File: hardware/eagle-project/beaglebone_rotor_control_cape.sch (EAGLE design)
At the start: 52 parts, among them IC1 TLC2264CDU, IC2 MCP4901, IC6 TLC2264CDU, Q1 SQ2348ES-T1-GE3, Q2 SQ2348ES-T1-GE3, Q3 SQ2348ES-T1-GE3, Q4 SQ2348ES-T1-GE3, Q5 SQ2348ES-T1-GE3, Q6 SQ2348ES-T1-GE3, U1 TMH0512S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

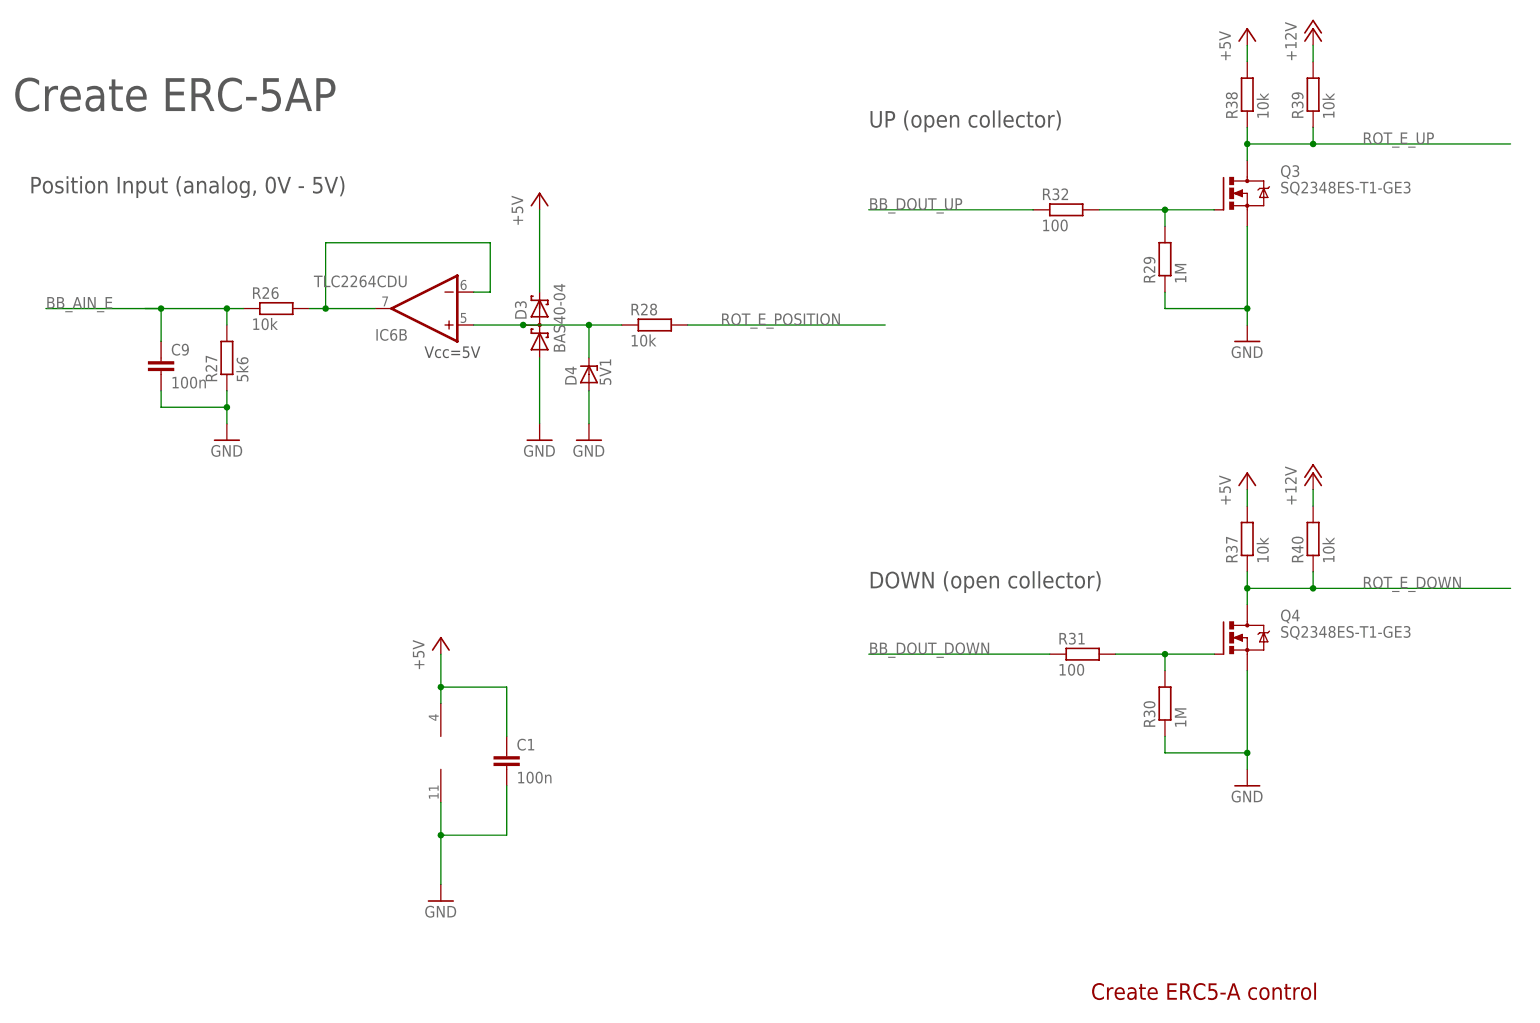
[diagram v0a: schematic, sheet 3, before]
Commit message: Optical tweaks for eagle schematic
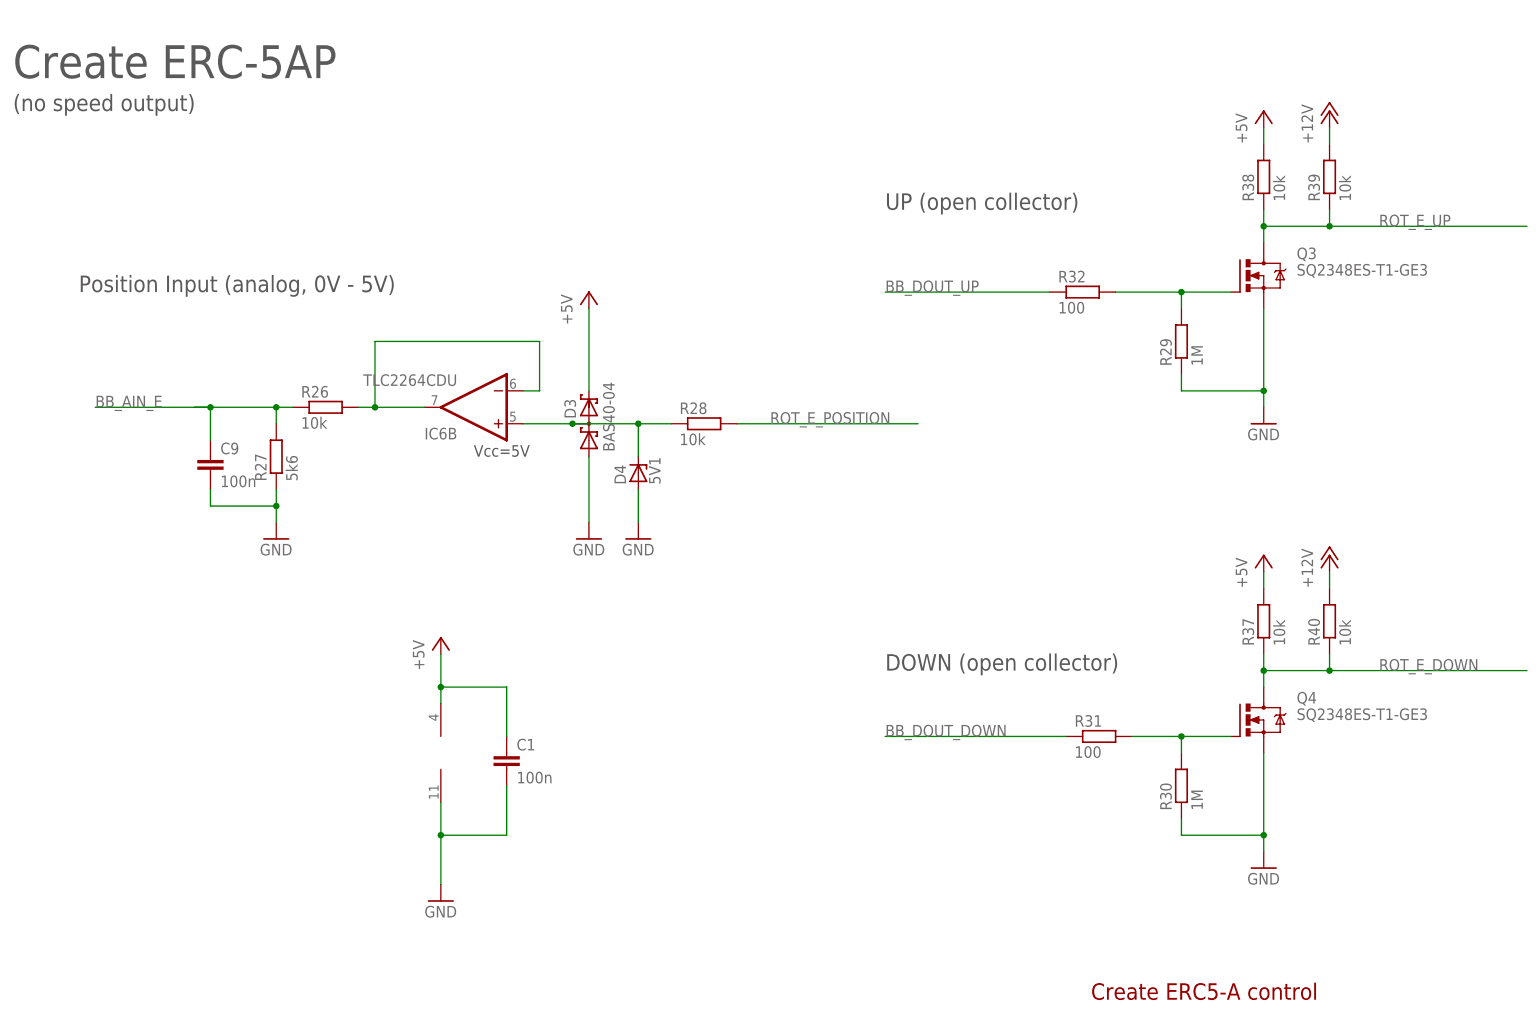
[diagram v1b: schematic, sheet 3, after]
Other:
- note added: "(no speed output)"
- moved on the sheet: C9, D3, D4, IC6B, Q3, Q4, R26, R27, R28, R29, R30, R31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

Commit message: Added serial interface chip to layout
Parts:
- removed R21: 100, rcl:R-EU_R0805
- added C10, C4, C5, C6, C8: 100n, rcl:C-EUC0603
- added IC3: MAX3232ESE, maxim:MAX3232ESE
- added R1, R8: 100, rcl:R-EU_R0805
- added X2: (no value), con-subd:F09VP
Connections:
- removed net BB_SPI0_D1: X1.I2C1_SDA
- removed net BB_SPI1_CS0: X1.SPI1_CS0
- removed net BB_SPI1_D0: X1.SPI1_DO
- removed net BB_SPI1_D1: X1.SPI1_DI
- removed net BB_SPI1_SCLK: X1.SPI1_SCLK
- removed net N$41: X1.EHRPWM2A
- removed net N$42: X1.GPIO1_14
- removed net N$4243: X1.GPIO2_1
- removed net N$43: X1.GPIO0_26
- removed net N$44: X1.GPIO1_12
- removed net N$8: R21.1
- new net BB_UART4_RX: R1.1, X1.UART4_RXD
- new net BB_UART4_TX: R8.1, X1.UART4_TXD
- new net N$16: C4.1, IC3G$1.C2+
- new net N$17: C4.2, IC3G$1.C2-
- new net N$18: C5.2, IC3G$1.C1-
- new net N$19: C5.1, IC3G$1.C1+
- new net N$20: C6.1, IC3G$1.V-
- new net N$21: C8.1, IC3G$1.V+
- new net N$22: IC3G$1.T1IN, R8.2
- new net N$25: IC3G$1.R1OUT, R1.2
- new net RS232_RX: IC3G$1.R1IN, X2.3
- new net RS232_TX: IC3G$1.T1OUT, X2.2
- net +3V3: now also C10.1, IC3P.VCC
- net GND: now also C10.2, C6.2, C8.2, IC3P.GND, X2.5
- net N$7: no longer R21.2
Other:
- note added: "Information: - the serial port is deactivated in normal operation"
- note added: "RS-232 interface"
- note removed: "P9.18"
